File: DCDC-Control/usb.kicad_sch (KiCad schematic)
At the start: 3 parts, among them J1 USB_C_Receptacle_USB2.0_16P

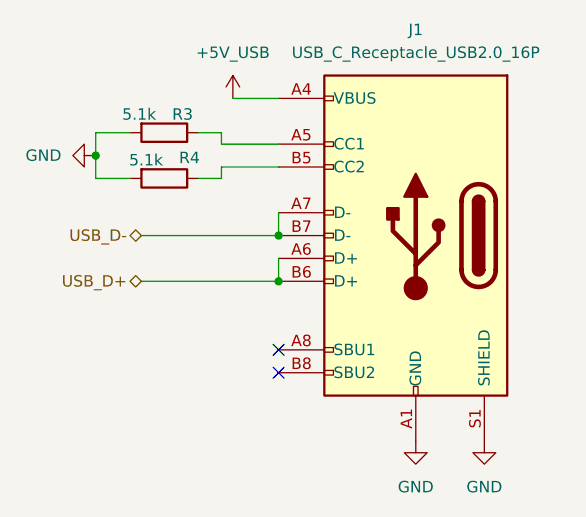
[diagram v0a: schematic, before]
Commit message: some DCDC schematics
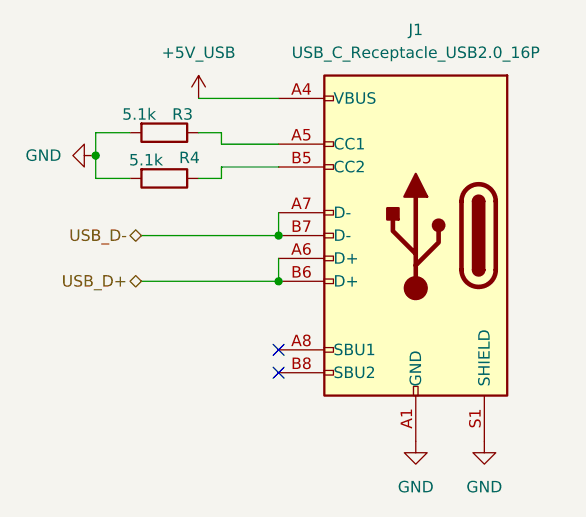
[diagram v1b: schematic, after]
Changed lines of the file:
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@@
 	(wire
 		(pts
-			(xy 139.7 81.28) (xy 144.78 81.28)
+			(xy 135.89 81.28) (xy 144.78 81.28)
 		)
 		(stroke
@@
 	(symbol
 		(lib_id "power:+5V")
-		(at 139.7 81.28 0)
+		(at 135.89 81.28 0)
 		(unit 1)
 		(exclude_from_sim no)
@@
 		(fields_autoplaced yes)
 		(property "Reference" "#PWR010"
-			(at 139.7 85.09 0)
+			(at 135.89 85.09 0)
 			(effects
 				(font
@@
 		)
 		(property "Value" "+5V_USB"
-			(at 139.7 76.2 0)
+			(at 135.89 76.2 0)
 			(effects
 				(font
@@
 		)
 		(property "Footprint" ""
-			(at 139.7 81.28 0)
+			(at 135.89 81.28 0)
 			(effects
 				(font
@@
 		)
 		(property "Datasheet" ""
-			(at 139.7 81.28 0)
+			(at 135.89 81.28 0)
 			(effects
 				(font
@@
 		)
 		(property "Description" "Power symbol creates a global label with name \"+5V\""
-			(at 139.7 81.28 0)
+			(at 135.89 81.28 0)
 			(effects
 				(font
